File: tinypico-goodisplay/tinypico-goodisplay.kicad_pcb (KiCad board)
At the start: 2 copper layers, 39.8 x 17.8 mm, 23 parts, among them Q1 Si1308, U1 TinypicoESP32_Symbol, U2 FPCConn

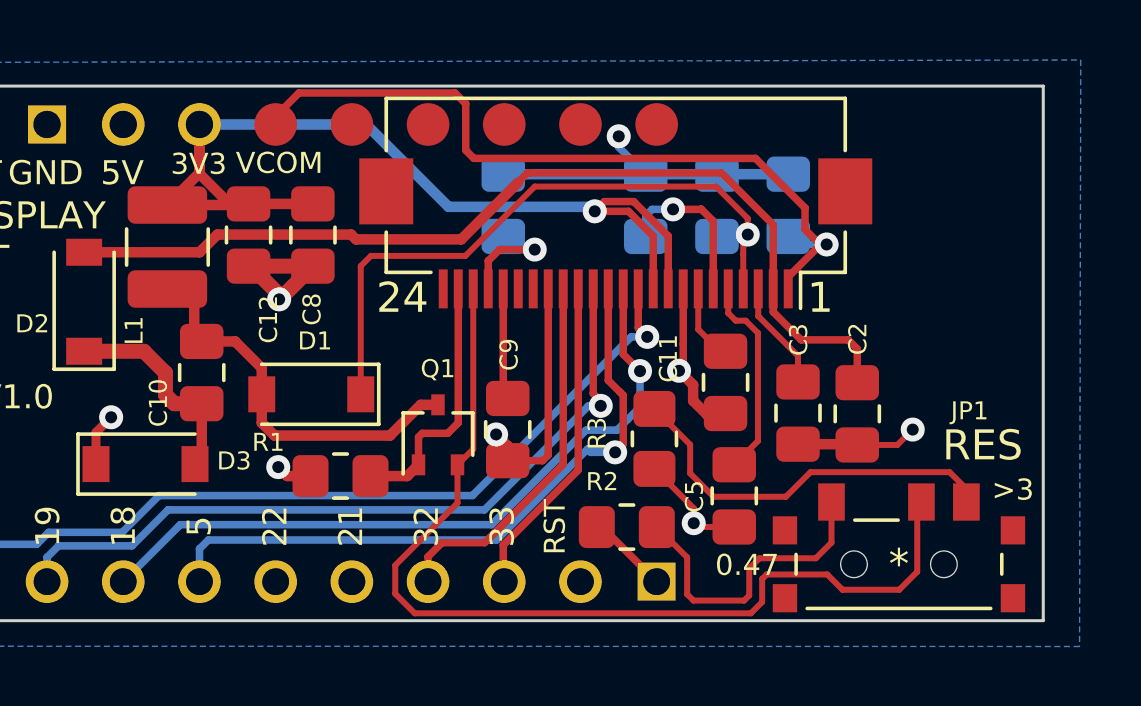
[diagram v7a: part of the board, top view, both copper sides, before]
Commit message: Do not exclude C8 from POS files
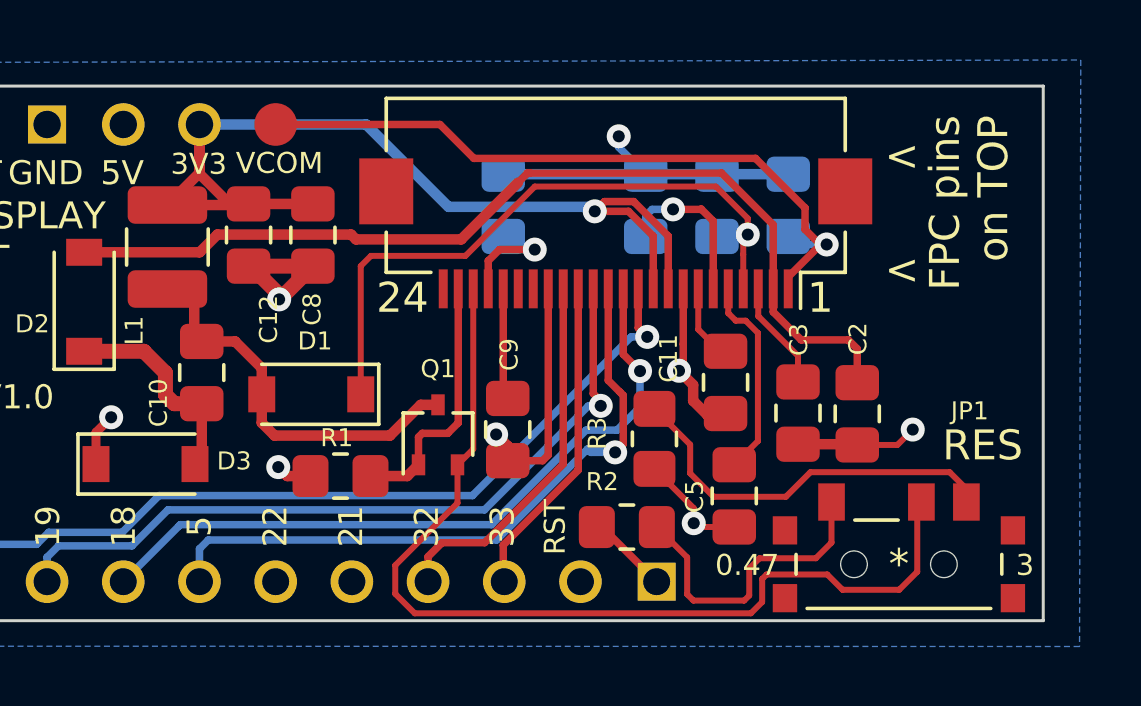
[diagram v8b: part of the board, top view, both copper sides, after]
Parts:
- U1: footprint Tinypico:TinyESP32 -> footprint:TinyESP32
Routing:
- net /VCOM: track 25.6 -> 24.0 mm
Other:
- board text added: "3"
- board text added: "<"
- board text added: "FPC pins on TOP"
- board text removed: ">3"
